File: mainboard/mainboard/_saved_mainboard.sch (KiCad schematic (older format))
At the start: 15 parts, among them U1 STM32F446RETx

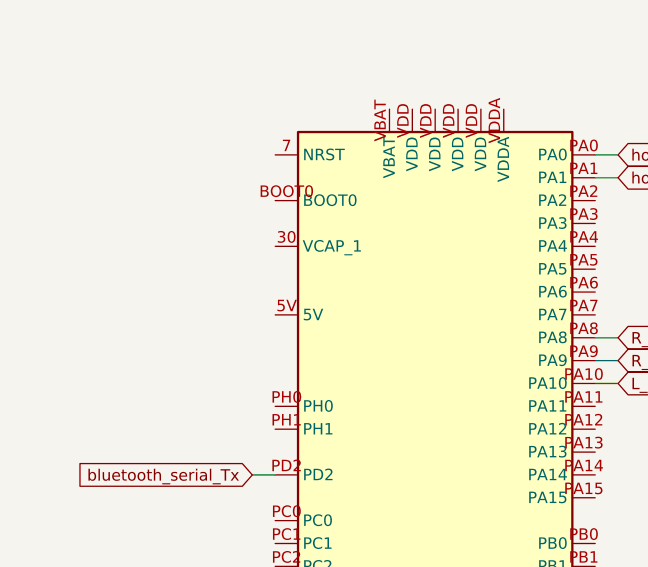
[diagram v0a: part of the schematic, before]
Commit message: started routing, added 5v
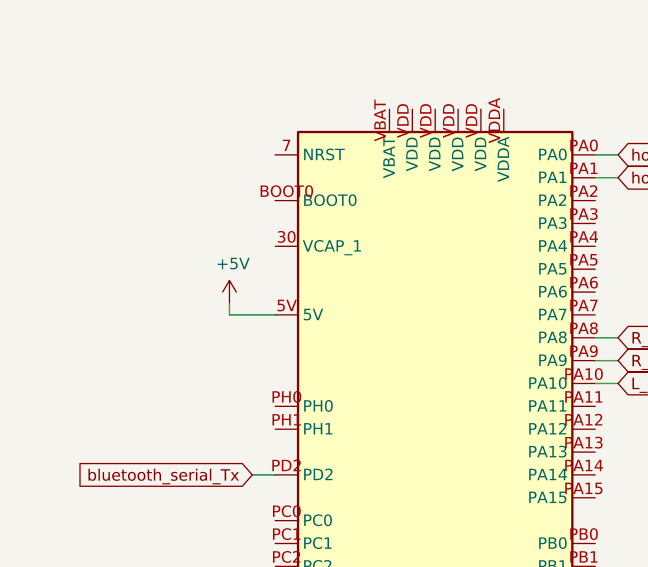
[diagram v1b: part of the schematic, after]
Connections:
- net +5V: now also U1.5V
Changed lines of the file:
@@
 Wire Wire Line
 	7550 1050 7550 1200
+$Comp
+L power:+5V #PWR?
+U 1 1 5D8A06EA
+P 1150 2300
+F 0 "#PWR?" H 1150 2150 50  0001 C CNN
+F 1 "+5V" H 1165 2473 50  0000 C CNN
+F 2 "" H 1150 2300 50  0001 C CNN
+F 3 "" H 1150 2300 50  0001 C CNN
+	1    1150 2300
+	1    0    0    -1
+$EndComp
+Wire Wire Line
+	1350 2350 1150 2350
+Wire Wire Line
+	1150 2350 1150 2300
 $EndSCHEMATC

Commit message: routed, checking...
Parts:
- added J7_btcomms_2: Conn_01x06, Connector_Molex:Molex_KK-254_AE-6410-06A_1x06_P2.54mm_Vertical, symbol Connector_Generic:Conn_01x06
- added R?: 2k, Resistor_THT:R_Axial_DIN0204_L3.6mm_D1.6mm_P5.08mm_Horizontal, symbol Device:R
- added R?: 1k, Resistor_THT:R_Axial_DIN0204_L3.6mm_D1.6mm_P5.08mm_Horizontal, symbol Device:R
- renumbered J_bt_comms1 to J1_btcomms_1, J_IMU1 to J2_IMU1, J_hoverboard_serial1 to J3_hoverboard_serial1, J_serial3 to J4_serial3, J_L_H_IN1 to J5_LEFT_HALL_IN, J_R_H_IN1 to J6_RIGHT_HALL_IN
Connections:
- net +5V: now also J7_btcomms_2.2 (Pin_2)
- net GND: now also U1.GND, J7_btcomms_2.3 (Pin_3), R?.1
- net bluetooth_serial_2_Rx: now reaches U1.PA2
- net bluetooth_serial_2_Rx: now also R?.1
- net bluetooth_serial_2_Tx: now reaches U1.PA3
- net bluetooth_serial_2_Tx: now also J7_btcomms_2.4 (Pin_4)
- net bluetooth_serial_Rx renamed bluetooth_serial_1_Rx
- net bluetooth_serial_Tx renamed bluetooth_serial_1_Tx
- new net: J7_btcomms_2.5 (Pin_5), R?.2, R?.2
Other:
- moved on the sheet: J5_LEFT_HALL_IN, J6_RIGHT_HALL_IN
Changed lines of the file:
@@
 hoverboard_serial_Rx
 Text GLabel 1250 4450 0    50   Input ~ 0
-bluetooth_serial_Rx
+bluetooth_serial_1_Rx
 Text GLabel 1250 3050 0    50   Input ~ 0
-bluetooth_serial_Tx
+bluetooth_serial_1_Tx
 Wire Wire Line
 	2850 2450 2750 2450
@@
 $EndComp
 $Comp
-L Connector_Generic:Conn_01x06 J_bt_comms1
+L Connector_Generic:Conn_01x06 J1_btcomms_1
 U 1 1 5D860DFC
 P 4100 6450
-F 0 "J_bt_comms1" V 4250 6200 50  0000 L CNN
+F 0 "J1_btcomms_1" V 4250 6200 50  0000 L CNN
 F 1 "Conn_01x06" V 4350 6200 50  0000 L CNN
 F 2 "Connector_Molex:Molex_KK-254_AE-6410-06A_1x06_P2.54mm_Vertical" H 4100 6450 50  0001 C CNN
@@
 $EndComp
 Text GLabel 4150 5700 0    50   Input ~ 0
-bluetooth_serial_Tx
+bluetooth_serial_1_Tx
 Text GLabel 4250 5550 0    50   Input ~ 0
-bluetooth_serial_Rx
+bluetooth_serial_1_Rx
 Wire Wire Line
 	4000 6000 4000 6250
@@
 	4300 5550 4300 5800
 $Comp
-L Connector_Generic:Conn_01x04 J_R_H_IN1
+L Connector_Generic:Conn_01x04 J6_RIGHT_HALL_IN
 U 1 1 5D87E470
-P 6000 5850
-F 0 "J_R_H_IN1" V 5873 5562 50  0000 R CNN
-F 1 "Conn_01x04" V 5964 5562 50  0000 R CNN
-F 2 "Connector_Molex:Molex_KK-254_AE-6410-04A_1x04_P2.54mm_Vertical" H 6000 5850 50  0001 C CNN
-F 3 "~" H 6000 5850 50  0001 C CNN
-	1    6000 5850
+P 9750 3100
+F 0 "J6_RIGHT_HALL_IN" V 9623 2812 50  0000 R CNN
+F 1 "Conn_01x04" V 9714 2812 50  0000 R CNN
+F 2 "Connector_Molex:Molex_KK-254_AE-6410-04A_1x04_P2.54mm_Vertical" H 9750 3100 50  0001 C CNN
+F 3 "~" H 9750 3100 50  0001 C CNN
+	1    9750 3100
 	0    -1   1    0
 $EndComp
-Text GLabel 5900 5200 0    50   Input ~ 0
+Text GLabel 9650 2450 0    50   Input ~ 0
 R_hall_A_in
-Text GLabel 5900 5350 0    50   Input ~ 0
+Text GLabel 9650 2600 0    50   Input ~ 0
 R_hall_B_in
-Text GLabel 5900 5500 0    50   Input ~ 0
+Text GLabel 9650 2750 0    50   Input ~ 0
 R_hall_C_in
 $Comp
 L power:GND #PWR06
 U 1 1 5D882210
-P 5650 5800
-F 0 "#PWR06" H 5650 5550 50  0001 C CNN
-F 1 "GND" H 5655 5627 50  0000 C CNN
-F 2 "" H 5650 5800 50  0001 C CNN
-F 3 "" H 5650 5800 50  0001 C CNN
-	1    5650 5800
-	1    0    0    -1
-$EndComp
-Wire Wire Line
-	5900 5200 6200 5200
-Wire Wire Line
-	6200 5200 6200 5650
-Wire Wire Line
-	6100 5650 6100 5350
-Wire Wire Line
-	6100 5350 5900 5350
-Wire Wire Line
-	6000 5650 6000 5500
-Wire Wire Line
-	6000 5500 5900 5500
-Wire Wire Line
-	5900 5650 5900 5600
-Wire Wire Line
-	5900 5600 5650 5600
-Wire Wire Line
-	5650 5600 5650 5800
-$Comp
-L Connector_Generic:Conn_01x04 J_L_H_IN1
+P 9400 3050
+F 0 "#PWR06" H 9400 2800 50  0001 C CNN
+F 1 "GND" H 9405 2877 50  0000 C CNN
+F 2 "" H 9400 3050 50  0001 C CNN
+F 3 "" H 9400 3050 50  0001 C CNN
+	1    9400 3050
+	1    0    0    -1
+$EndComp
+Wire Wire Line
+	9650 2450 9950 2450
+Wire Wire Line
+	9950 2450 9950 2900
+Wire Wire Line
+	9850 2900 9850 2600
+Wire Wire Line
+	9850 2600 9650 2600
+Wire Wire Line
+	9750 2900 9750 2750
+Wire Wire Line
+	9750 2750 9650 2750
+Wire Wire Line
+	9650 2900 9650 2850
+Wire Wire Line
+	9650 2850 9400 2850
+Wire Wire Line
+	9400 2850 9400 3050
+$Comp
+L Connector_Generic:Conn_01x04 J5_LEFT_HALL_IN
 U 1 1 5D886892
-P 7350 5850
-F 0 "J_L_H_IN1" V 7223 5562 50  0000 R CNN
-F 1 "Conn_01x04" V 7314 5562 50  0000 R CNN
-F 2 "Connector_Molex:Molex_KK-254_AE-6410-04A_1x04_P2.54mm_Vertical" H 7350 5850 50  0001 C CNN
-F 3 "~" H 7350 5850 50  0001 C CNN
-	1    7350 5850
+P 9750 1900
+F 0 "J5_LEFT_HALL_IN" V 9623 1612 50  0000 R CNN
+F 1 "Conn_01x04" V 9714 1612 50  0000 R CNN
+F 2 "Connector_Molex:Molex_KK-254_AE-6410-04A_1x04_P2.54mm_Vertical" H 9750 1900 50  0001 C CNN
+F 3 "~" H 9750 1900 50  0001 C CNN
+	1    9750 1900
 	0    -1   1    0
 $EndComp
-Text GLabel 7250 5200 0    50   Input ~ 0
+Text GLabel 9650 1250 0    50   Input ~ 0
 L_hall_A_in
-Text GLabel 7250 5350 0    50   Input ~ 0
+Text GLabel 9650 1400 0    50   Input ~ 0
 L_hall_B_in
-Text GLabel 7250 5500 0    50   Input ~ 0
+Text GLabel 9650 1550 0    50   Input ~ 0
 L_hall_C_in
 $Comp
 L power:GND #PWR014
 U 1 1 5D88689C
-P 7000 5800
-F 0 "#PWR014" H 7000 5550 50  0001 C CNN
-F 1 "GND" H 7005 5627 50  0000 C CNN
-F 2 "" H 7000 5800 50  0001 C CNN
-F 3 "" H 7000 5800 50  0001 C CNN
-	1    7000 5800
-	1    0    0    -1
-$EndComp
-Wire Wire Line
-	7250 5200 7550 5200
-Wire Wire Line
-	7550 5200 7550 5650
-Wire Wire Line
-	7450 5650 7450 5350
-Wire Wire Line
-	7450 5350 7250 5350
-Wire Wire Line
-	7350 5650 7350 5500
-Wire Wire Line
-	7350 5500 7250 5500
-Wire Wire Line
-	7250 5650 7250 5600
-Wire Wire Line
-	7250 5600 7000 5600
-Wire Wire Line
-	7000 5600 7000 5800
-$Comp
-L Connector_Generic:Conn_01x08 J_IMU1
+P 9400 1850
+F 0 "#PWR014" H 9400 1600 50  0001 C CNN
+F 1 "GND" H 9405 1677 50  0000 C CNN
+F 2 "" H 9400 1850 50  0001 C CNN
+F 3 "" H 9400 1850 50  0001 C CNN
+	1    9400 1850
+	1    0    0    -1
+$EndComp
+Wire Wire Line
+	9650 1250 9950 1250
+Wire Wire Line
+	9950 1250 9950 1700
+Wire Wire Line
+	9850 1700 9850 1400
+Wire Wire Line
+	9850 1400 9650 1400
+Wire Wire Line
+	9750 1700 9750 1550
+Wire Wire Line
+	9750 1550 9650 1550
+Wire Wire Line
+	9650 1700 9650 1650
+Wire Wire Line
+	9650 1650 9400 1650
+Wire Wire Line
+	9400 1650 9400 1850
+$Comp
+L Connector_Generic:Conn_01x08 J2_IMU1
 U 1 1 5D88811D
 P 2100 6350
-F 0 "J_IMU1" V 2317 6296 50  0000 C CNN
+F 0 "J2_IMU1" V 2317 6296 50  0000 C CNN
 F 1 "Conn_01x08" V 2226 6296 50  0000 C CNN
 F 2 "Connector_Molex:Molex_KK-254_AE-6410-08A_1x08_P2.54mm_Vertical" H 2100 6350 50  0001 C CNN
@@
 	2850 4250 2750 4250
 $Comp
-L Connector_Generic:Conn_01x03 J_hoverboard_serial1
+L Connector_Generic:Conn_01x03 J3_hoverboard_serial1
 U 1 1 5D89FEC7
 P 5900 1400
-F 0 "J_hoverboard_serial1" H 5819 1075 50  0000 C CNN
+F 0 "J3_hoverboard_serial1" H 5819 1075 50  0000 C CNN
 F 1 "Conn_01x03" H 5819 1166 50  0000 C CNN
 F 2 "Connector_Molex:Molex_KK-254_AE-6410-03A_1x03_P2.54mm_Vertical" H 5900 1400 50  0001 C CNN
@@
 	1350 4350 1200 4350
 $Comp
-L Connector_Generic:Conn_01x04 J_serial3
+L Connector_Generic:Conn_01x04 J4_serial3
 U 1 1 5D8A9BEB
 P 7750 1400
-F 0 "J_serial3" H 8000 1300 50  0000 C CNN
+F 0 "J4_serial3" H 8150 1300 50  0000 C CNN
 F 1 "Conn_01x04" H 8050 1400 50  0000 C CNN
 F 2 "" H 7750 1400 50  0001 C CNN
@@
 Wire Wire Line
 	1150 2350 1150 2300
+$Comp
+L Device:R R?
+U 1 1 5D8EE4A7
+P 6150 6150
+F 0 "R?" V 5950 6200 50  0000 C CNN
+F 1 "2k" V 6050 6200 50  0000 C CNN
+F 2 "Resistor_THT:R_Axial_DIN0204_L3.6mm_D1.6mm_P5.08mm_Horizontal" V 6080 6150 50  0001 C CNN
+F 3 "~" H 6150 6150 50  0001 C CNN
+	1    6150 6150
+	0    1    1    0
+$EndComp
+$Comp
+L Device:R R?
+U 1 1 5D8EE4AE
+P 5900 5950
+F 0 "R?" H 5970 5996 50  0000 L CNN
+F 1 "1k" H 5970 5905 50  0000 L CNN
+F 2 "Resistor_THT:R_Axial_DIN0204_L3.6mm_D1.6mm_P5.08mm_Horizontal" V 5830 5950 50  0001 C CNN
+F 3 "~" H 5900 5950 50  0001 C CNN
+	1    5900 5950
+	1    0    0    -1
+$EndComp
+$Comp
+L Connector_Generic:Conn_01x06 J7_btcomms_2
+U 1 1 5D8EE4B5
+P 5700 6450
+F 0 "J7_btcomms_2" V 5850 6200 50  0000 L CNN
+F 1 "Conn_01x06" V 5950 6200 50  0000 L CNN
+F 2 "Connector_Molex:Molex_KK-254_AE-6410-06A_1x06_P2.54mm_Vertical" H 5700 6450 50  0001 C CNN
+F 3 "~" H 5700 6450 50  0001 C CNN
+	1    5700 6450
+	0    -1   1    0
+$EndComp
+$Comp
+L power:+5V #PWR?
+U 1 1 5D8EE4BC
+P 5600 6000
+F 0 "#PWR?" H 5600 5850 50  0001 C CNN
+F 1 "+5V" H 5615 6173 50  0000 C CNN
+F 2 "" H 5600 6000 50  0001 C CNN
+F 3 "" H 5600 6000 50  0001 C CNN
+	1    5600 6000
+	1    0    0    -1
+$EndComp
+$Comp
+L power:GND #PWR?
+U 1 1 5D8EE4C2
+P 5300 6250
+F 0 "#PWR?" H 5300 6000 50  0001 C CNN
+F 1 "GND" H 5305 6077 50  0000 C CNN
+F 2 "" H 5300 6250 50  0001 C CNN
+F 3 "" H 5300 6250 50  0001 C CNN
+	1    5300 6250
+	1    0    0    -1
+$EndComp
+Text GLabel 5750 5700 0    50   Input ~ 0
+bluetooth_serial_2_Tx
+Text GLabel 5850 5550 0    50   Input ~ 0
+bluetooth_serial_2_Rx
+Wire Wire Line
+	5600 6000 5600 6250
+Wire Wire Line
+	5800 6250 5800 5700
+Wire Wire Line
+	5800 5700 5750 5700
+Wire Wire Line
+	5900 6250 5900 6150
+Wire Wire Line
+	6000 6150 5900 6150
+Connection ~ 5900 6150
+Wire Wire Line
+	5900 6150 5900 6100
+Wire Wire Line
+	5700 6250 5700 6150
+Wire Wire Line
+	5700 6150 5300 6150
+Wire Wire Line
+	5300 6150 5300 6250
+$Comp
+L power:GND #PWR?
+U 1 1 5D8EE4D4
+P 6450 6150
+F 0 "#PWR?" H 6450 5900 50  0001 C CNN
+F 1 "GND" H 6455 5977 50  0000 C CNN
+F 2 "" H 6450 6150 50  0001 C CNN
+F 3 "" H 6450 6150 50  0001 C CNN
+	1    6450 6150
+	1    0    0    -1
+$EndComp
+Wire Wire Line
+	6300 6150 6450 6150
+Wire Wire Line
+	5850 5550 5900 5550
+Wire Wire Line
+	5900 5550 5900 5800
+Text GLabel 2850 1950 2    50   Input ~ 0
+bluetooth_serial_2_Tx
+Text GLabel 2850 1850 2    50   Input ~ 0
+bluetooth_serial_2_Rx
+Wire Wire Line
+	2850 1950 2750 1950
+Wire Wire Line
+	2850 1850 2750 1850
+$Comp
+L power:GND #PWR?
+U 1 1 5D91A189
+P 2400 5100
+F 0 "#PWR?" H 2400 4850 50  0001 C CNN
+F 1 "GND" H 2405 4927 50  0000 C CNN
+F 2 "" H 2400 5100 50  0001 C CNN
+F 3 "" H 2400 5100 50  0001 C CNN
+	1    2400 5100
+	1    0    0    -1
+$EndComp
+Wire Wire Line
+	2400 4950 2400 5100
 $EndSCHEMATC

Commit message: ready for first cut
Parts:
- added H1, H2, H3: MountingHole, MountingHole:MountingHole_3.2mm_M3, symbol Mechanical:MountingHole
- J1_btcomms_1, J7_btcomms_2: footprint Connector_Molex:Molex_KK-254_AE-6410-06A_1x06_P2.54mm_Vertical -> kicad_footprints:Molex_KK-254_AE-6410-06A_1x06_P2.54mm_Vertical
- J2_IMU1: footprint Connector_Molex:Molex_KK-254_AE-6410-08A_1x08_P2.54mm_Vertical -> kicad_footprints:Molex_KK-254_AE-6410-08A_1x08_P2.54mm_Vertical
- J3_hoverboard_serial1: footprint Connector_Molex:Molex_KK-254_AE-6410-03A_1x03_P2.54mm_Vertical -> kicad_footprints:Molex_KK-254_AE-6410-03A_1x03_P2.54mm_Vertical
- J4_serial3: footprint (none) -> kicad_footprints:Molex_KK-254_AE-6410-04A_1x04_P2.54mm_Vertical
- J5_LEFT_HALL_IN1: renamed from J5_LEFT_HALL_IN; footprint Connector_Molex:Molex_KK-254_AE-6410-04A_1x04_P2.54mm_Vertical -> kicad_footprints:Molex_KK-254_AE-6410-04A_1x04_P2.54mm_Vertical
- J6_RIGHT_HALL_IN1: renamed from J6_RIGHT_HALL_IN; footprint Connector_Molex:Molex_KK-254_AE-6410-04A_1x04_P2.54mm_Vertical -> kicad_footprints:Molex_KK-254_AE-6410-04A_1x04_P2.54mm_Vertical
- R1, R2: footprint Resistor_THT:R_Axial_DIN0204_L3.6mm_D1.6mm_P5.08mm_Horizontal -> kicad_footprints:R_Axial_DIN0204_L3.6mm_D1.6mm_P5.08mm_Horizontal
- R3, R4: renamed from R?; footprint Resistor_THT:R_Axial_DIN0204_L3.6mm_D1.6mm_P5.08mm_Horizontal -> kicad_footprints:R_Axial_DIN0204_L3.6mm_D1.6mm_P5.08mm_Horizontal
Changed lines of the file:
@@
 F 0 "R2" V 4350 6200 50  0000 C CNN
 F 1 "2k" V 4450 6200 50  0000 C CNN
-F 2 "Resistor_THT:R_Axial_DIN0204_L3.6mm_D1.6mm_P5.08mm_Horizontal" V 4480 6150 50  0001 C CNN
+F 2 "kicad_footprints:R_Axial_DIN0204_L3.6mm_D1.6mm_P5.08mm_Horizontal" V 4480 6150 50  0001 C CNN
 F 3 "~" H 4550 6150 50  0001 C CNN
 	1    4550 6150
@@
 F 0 "R1" H 4370 5996 50  0000 L CNN
 F 1 "1k" H 4370 5905 50  0000 L CNN
-F 2 "Resistor_THT:R_Axial_DIN0204_L3.6mm_D1.6mm_P5.08mm_Horizontal" V 4230 5950 50  0001 C CNN
+F 2 "kicad_footprints:R_Axial_DIN0204_L3.6mm_D1.6mm_P5.08mm_Horizontal" V 4230 5950 50  0001 C CNN
 F 3 "~" H 4300 5950 50  0001 C CNN
 	1    4300 5950
@@
 F 0 "J1_btcomms_1" V 4250 6200 50  0000 L CNN
 F 1 "Conn_01x06" V 4350 6200 50  0000 L CNN
-F 2 "Connector_Molex:Molex_KK-254_AE-6410-06A_1x06_P2.54mm_Vertical" H 4100 6450 50  0001 C CNN
+F 2 "kicad_footprints:Molex_KK-254_AE-6410-06A_1x06_P2.54mm_Vertical" H 4100 6450 50  0001 C CNN
 F 3 "~" H 4100 6450 50  0001 C CNN
 	1    4100 6450
@@
 	4300 5550 4300 5800
 $Comp
-L Connector_Generic:Conn_01x04 J6_RIGHT_HALL_IN
+L Connector_Generic:Conn_01x04 J6_RIGHT_HALL_IN1
 U 1 1 5D87E470
 P 9750 3100
-F 0 "J6_RIGHT_HALL_IN" V 9623 2812 50  0000 R CNN
+F 0 "J6_RIGHT_HALL_IN1" V 9623 2812 50  0000 R CNN
 F 1 "Conn_01x04" V 9714 2812 50  0000 R CNN
-F 2 "Connector_Molex:Molex_KK-254_AE-6410-04A_1x04_P2.54mm_Vertical" H 9750 3100 50  0001 C CNN
+F 2 "kicad_footprints:Molex_KK-254_AE-6410-04A_1x04_P2.54mm_Vertical" H 9750 3100 50  0001 C CNN
 F 3 "~" H 9750 3100 50  0001 C CNN
 	1    9750 3100
@@
 	9400 2850 9400 3050
 $Comp
-L Connector_Generic:Conn_01x04 J5_LEFT_HALL_IN
+L Connector_Generic:Conn_01x04 J5_LEFT_HALL_IN1
 U 1 1 5D886892
 P 9750 1900
-F 0 "J5_LEFT_HALL_IN" V 9623 1612 50  0000 R CNN
+F 0 "J5_LEFT_HALL_IN1" V 9623 1612 50  0000 R CNN
 F 1 "Conn_01x04" V 9714 1612 50  0000 R CNN
-F 2 "Connector_Molex:Molex_KK-254_AE-6410-04A_1x04_P2.54mm_Vertical" H 9750 1900 50  0001 C CNN
+F 2 "kicad_footprints:Molex_KK-254_AE-6410-04A_1x04_P2.54mm_Vertical" H 9750 1900 50  0001 C CNN
 F 3 "~" H 9750 1900 50  0001 C CNN
 	1    9750 1900
@@
 F 0 "J2_IMU1" V 2317 6296 50  0000 C CNN
 F 1 "Conn_01x08" V 2226 6296 50  0000 C CNN
-F 2 "Connector_Molex:Molex_KK-254_AE-6410-08A_1x08_P2.54mm_Vertical" H 2100 6350 50  0001 C CNN
+F 2 "kicad_footprints:Molex_KK-254_AE-6410-08A_1x08_P2.54mm_Vertical" H 2100 6350 50  0001 C CNN
 F 3 "~" H 2100 6350 50  0001 C CNN
 	1    2100 6350
@@
 F 0 "J3_hoverboard_serial1" H 5819 1075 50  0000 C CNN
 F 1 "Conn_01x03" H 5819 1166 50  0000 C CNN
-F 2 "Connector_Molex:Molex_KK-254_AE-6410-03A_1x03_P2.54mm_Vertical" H 5900 1400 50  0001 C CNN
+F 2 "kicad_footprints:Molex_KK-254_AE-6410-03A_1x03_P2.54mm_Vertical" H 5900 1400 50  0001 C CNN
 F 3 "~" H 5900 1400 50  0001 C CNN
 	1    5900 1400
@@
 F 0 "J4_serial3" H 8150 1300 50  0000 C CNN
 F 1 "Conn_01x04" H 8050 1400 50  0000 C CNN
-F 2 "" H 7750 1400 50  0001 C CNN
+F 2 "kicad_footprints:Molex_KK-254_AE-6410-04A_1x04_P2.54mm_Vertical" H 7750 1400 50  0001 C CNN
 F 3 "~" H 7750 1400 50  0001 C CNN
 	1    7750 1400
@@
 	7550 1050 7550 1200
 $Comp
-L power:+5V #PWR?
+L power:+5V #PWR0102
 U 1 1 5D8A06EA
 P 1150 2300
-F 0 "#PWR?" H 1150 2150 50  0001 C CNN
+F 0 "#PWR0102" H 1150 2150 50  0001 C CNN
 F 1 "+5V" H 1165 2473 50  0000 C CNN
 F 2 "" H 1150 2300 50  0001 C CNN
@@
 	1150 2350 1150 2300
 $Comp
-L Device:R R?
+L Device:R R4
 U 1 1 5D8EE4A7
 P 6150 6150
-F 0 "R?" V 5950 6200 50  0000 C CNN
+F 0 "R4" V 5950 6200 50  0000 C CNN
 F 1 "2k" V 6050 6200 50  0000 C CNN
-F 2 "Resistor_THT:R_Axial_DIN0204_L3.6mm_D1.6mm_P5.08mm_Horizontal" V 6080 6150 50  0001 C CNN
+F 2 "kicad_footprints:R_Axial_DIN0204_L3.6mm_D1.6mm_P5.08mm_Horizontal" V 6080 6150 50  0001 C CNN
 F 3 "~" H 6150 6150 50  0001 C CNN
 	1    6150 6150
@@
 $EndComp
 $Comp
-L Device:R R?
+L Device:R R3
 U 1 1 5D8EE4AE
 P 5900 5950
-F 0 "R?" H 5970 5996 50  0000 L CNN
+F 0 "R3" H 5970 5996 50  0000 L CNN
 F 1 "1k" H 5970 5905 50  0000 L CNN
-F 2 "Resistor_THT:R_Axial_DIN0204_L3.6mm_D1.6mm_P5.08mm_Horizontal" V 5830 5950 50  0001 C CNN
+F 2 "kicad_footprints:R_Axial_DIN0204_L3.6mm_D1.6mm_P5.08mm_Horizontal" V 5830 5950 50  0001 C CNN
 F 3 "~" H 5900 5950 50  0001 C CNN
 	1    5900 5950
@@
 F 0 "J7_btcomms_2" V 5850 6200 50  0000 L CNN
 F 1 "Conn_01x06" V 5950 6200 50  0000 L CNN
-F 2 "Connector_Molex:Molex_KK-254_AE-6410-06A_1x06_P2.54mm_Vertical" H 5700 6450 50  0001 C CNN
+F 2 "kicad_footprints:Molex_KK-254_AE-6410-06A_1x06_P2.54mm_Vertical" H 5700 6450 50  0001 C CNN
 F 3 "~" H 5700 6450 50  0001 C CNN
 	1    5700 6450
@@
 $EndComp
 $Comp
-L power:+5V #PWR?
+L power:+5V #PWR0103
 U 1 1 5D8EE4BC
 P 5600 6000
-F 0 "#PWR?" H 5600 5850 50  0001 C CNN
+F 0 "#PWR0103" H 5600 5850 50  0001 C CNN
 F 1 "+5V" H 5615 6173 50  0000 C CNN
 F 2 "" H 5600 6000 50  0001 C CNN
@@
 $EndComp
 $Comp
-L power:GND #PWR?
+L power:GND #PWR0104
 U 1 1 5D8EE4C2
 P 5300 6250
-F 0 "#PWR?" H 5300 6000 50  0001 C CNN
+F 0 "#PWR0104" H 5300 6000 50  0001 C CNN
 F 1 "GND" H 5305 6077 50  0000 C CNN
 F 2 "" H 5300 6250 50  0001 C CNN
@@
 	5300 6150 5300 6250
 $Comp
-L power:GND #PWR?
+L power:GND #PWR0105
 U 1 1 5D8EE4D4
 P 6450 6150
-F 0 "#PWR?" H 6450 5900 50  0001 C CNN
+F 0 "#PWR0105" H 6450 5900 50  0001 C CNN
 F 1 "GND" H 6455 5977 50  0000 C CNN
 F 2 "" H 6450 6150 50  0001 C CNN
@@
 	2850 1850 2750 1850
 $Comp
-L power:GND #PWR?
+L power:GND #PWR0106
 U 1 1 5D91A189
 P 2400 5100
-F 0 "#PWR?" H 2400 4850 50  0001 C CNN
+F 0 "#PWR0106" H 2400 4850 50  0001 C CNN
 F 1 "GND" H 2405 4927 50  0000 C CNN
 F 2 "" H 2400 5100 50  0001 C CNN
@@
 Wire Wire Line
 	2400 4950 2400 5100
+$Comp
+L Mechanical:MountingHole H1
+U 1 1 5D92068C
+P 8500 650
+F 0 "H1" H 8600 696 50  0000 L CNN
+F 1 "MountingHole" H 8600 605 50  0000 L CNN
+F 2 "MountingHole:MountingHole_3.2mm_M3" H 8500 650 50  0001 C CNN
+F 3 "~" H 8500 650 50  0001 C CNN
+	1    8500 650
+	1    0    0    -1
+$EndComp
+$Comp
+L Mechanical:MountingHole H2
+U 1 1 5D9206E8
+P 8500 850
+F 0 "H2" H 8600 896 50  0000 L CNN
+F 1 "MountingHole" H 8600 805 50  0000 L CNN
+F 2 "MountingHole:MountingHole_3.2mm_M3" H 8500 850 50  0001 C CNN
+F 3 "~" H 8500 850 50  0001 C CNN
+	1    8500 850
+	1    0    0    -1
+$EndComp
+$Comp
+L Mechanical:MountingHole H3
+U 1 1 5D920A4A
+P 8500 1050
+F 0 "H3" H 8600 1096 50  0000 L CNN
+F 1 "MountingHole" H 8600 1005 50  0000 L CNN
+F 2 "MountingHole:MountingHole_3.2mm_M3" H 8500 1050 50  0001 C CNN
+F 3 "~" H 8500 1050 50  0001 C CNN
+	1    8500 1050
+	1    0    0    -1
+$EndComp
 $EndSCHEMATC
